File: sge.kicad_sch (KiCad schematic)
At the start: 23 parts, among them IC6 315-5660

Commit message: Enlarge some footprints, fix unwanted A/D ground connections.
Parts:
- IC6: footprint Package_QFP:LQFP-208_28x28mm_P0.5mm -> Neptune:QFP-208_28x28_Pitch0.5mm
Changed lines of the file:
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@@
       (effects (font (size 5 5)))
     )
-    (property "Footprint" "Package_QFP:LQFP-208_28x28mm_P0.5mm" (at 212.09 135.89 0)
+    (property "Footprint" "Neptune:QFP-208_28x28_Pitch0.5mm" (at 212.09 135.89 0)
       (effects (font (size 1.27 1.27)) hide)
     )

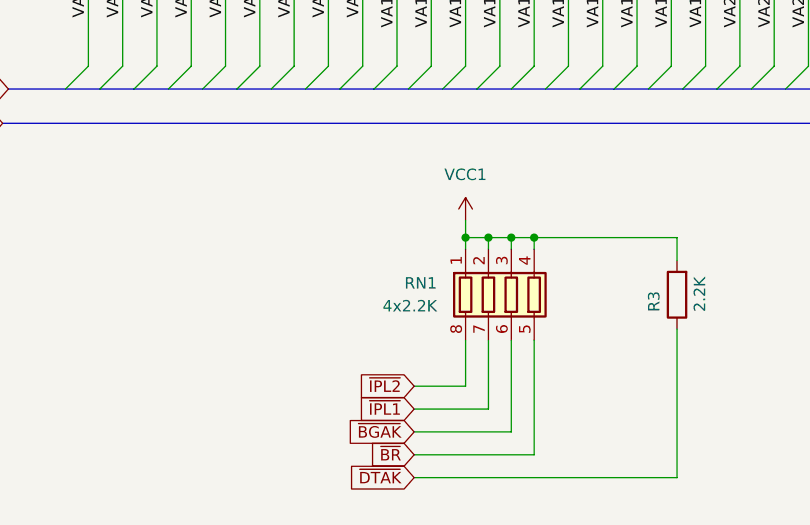
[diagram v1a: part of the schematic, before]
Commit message: Renumber "missing" resistor pack.
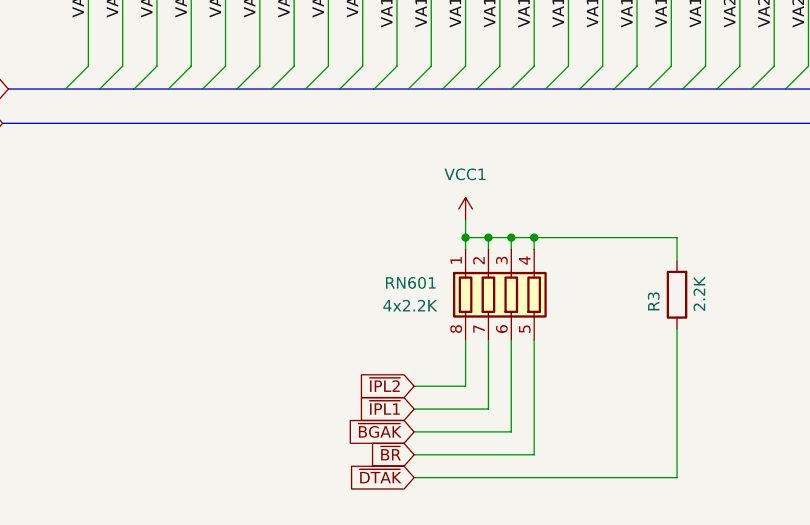
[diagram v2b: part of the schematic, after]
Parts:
- renumbered RN1 to RN601
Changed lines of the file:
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@@
   (symbol (lib_id "Device:R_Pack04") (at 127 256.54 0) (mirror x) (unit 1)
     (in_bom yes) (on_board yes) (dnp no)
-    (property "Reference" "RN1" (at 118.745 255.27 0)
+    (property "Reference" "RN601" (at 118.745 255.27 0)
       (effects (font (size 1.27 1.27)) (justify right))
     )
@@
       (project "Neptune"
         (path "/bcc23b51-b742-4ae5-9dd6-d96a24058944/0d895458-d3d0-4635-bde5-e15500822f5f"
-          (reference "RN1") (unit 1)
+          (reference "RN601") (unit 1)
         )
       )

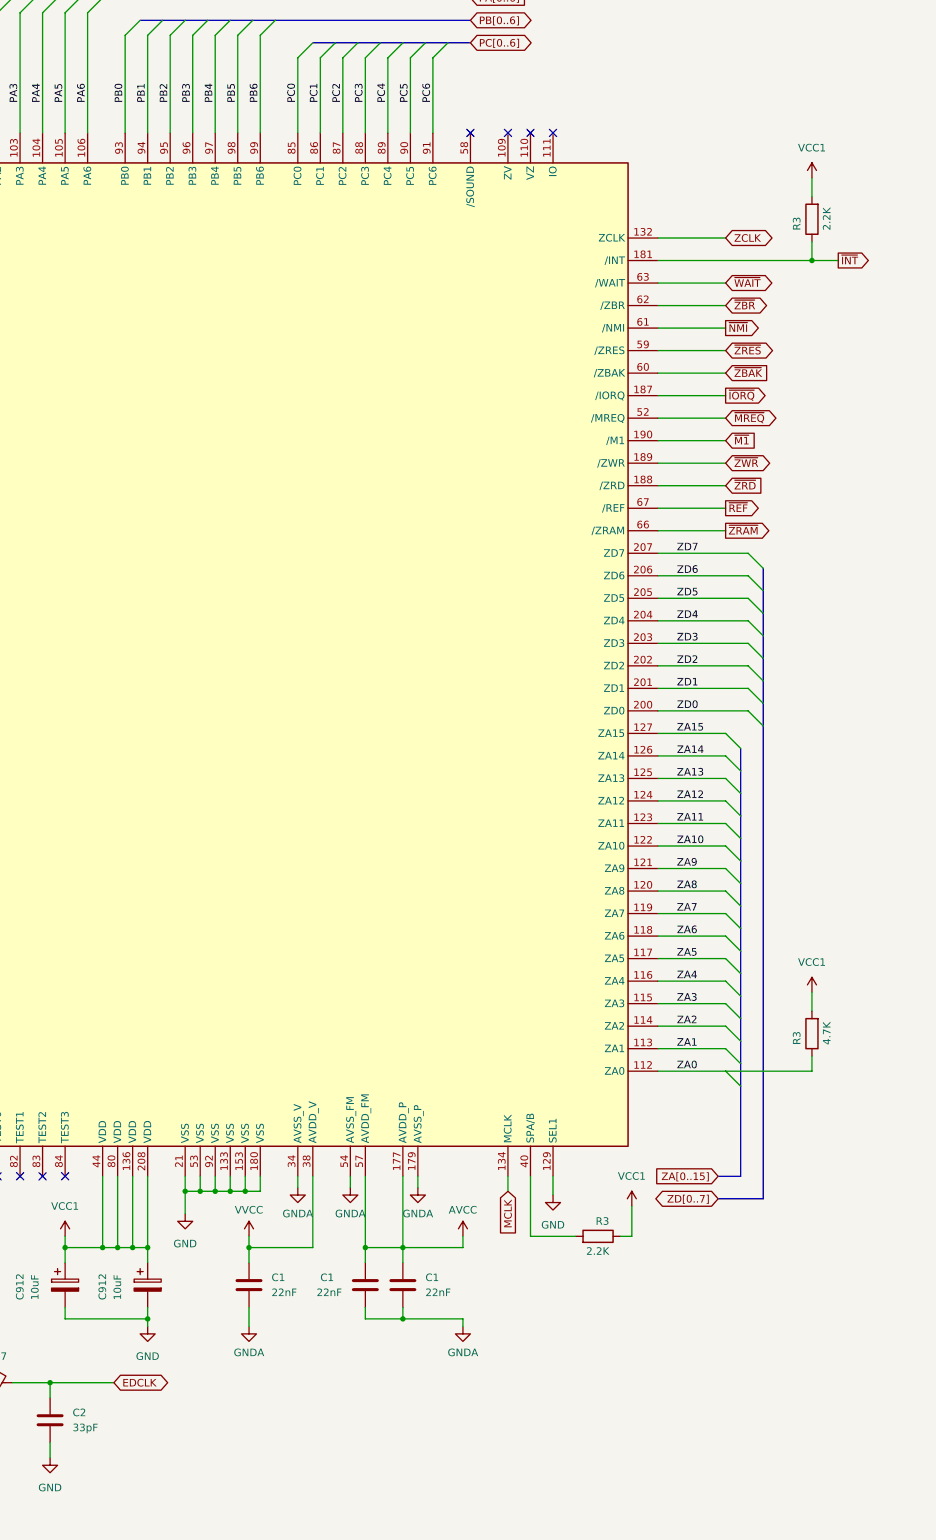
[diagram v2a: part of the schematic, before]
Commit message: Add/correct MD PAL timing caps.
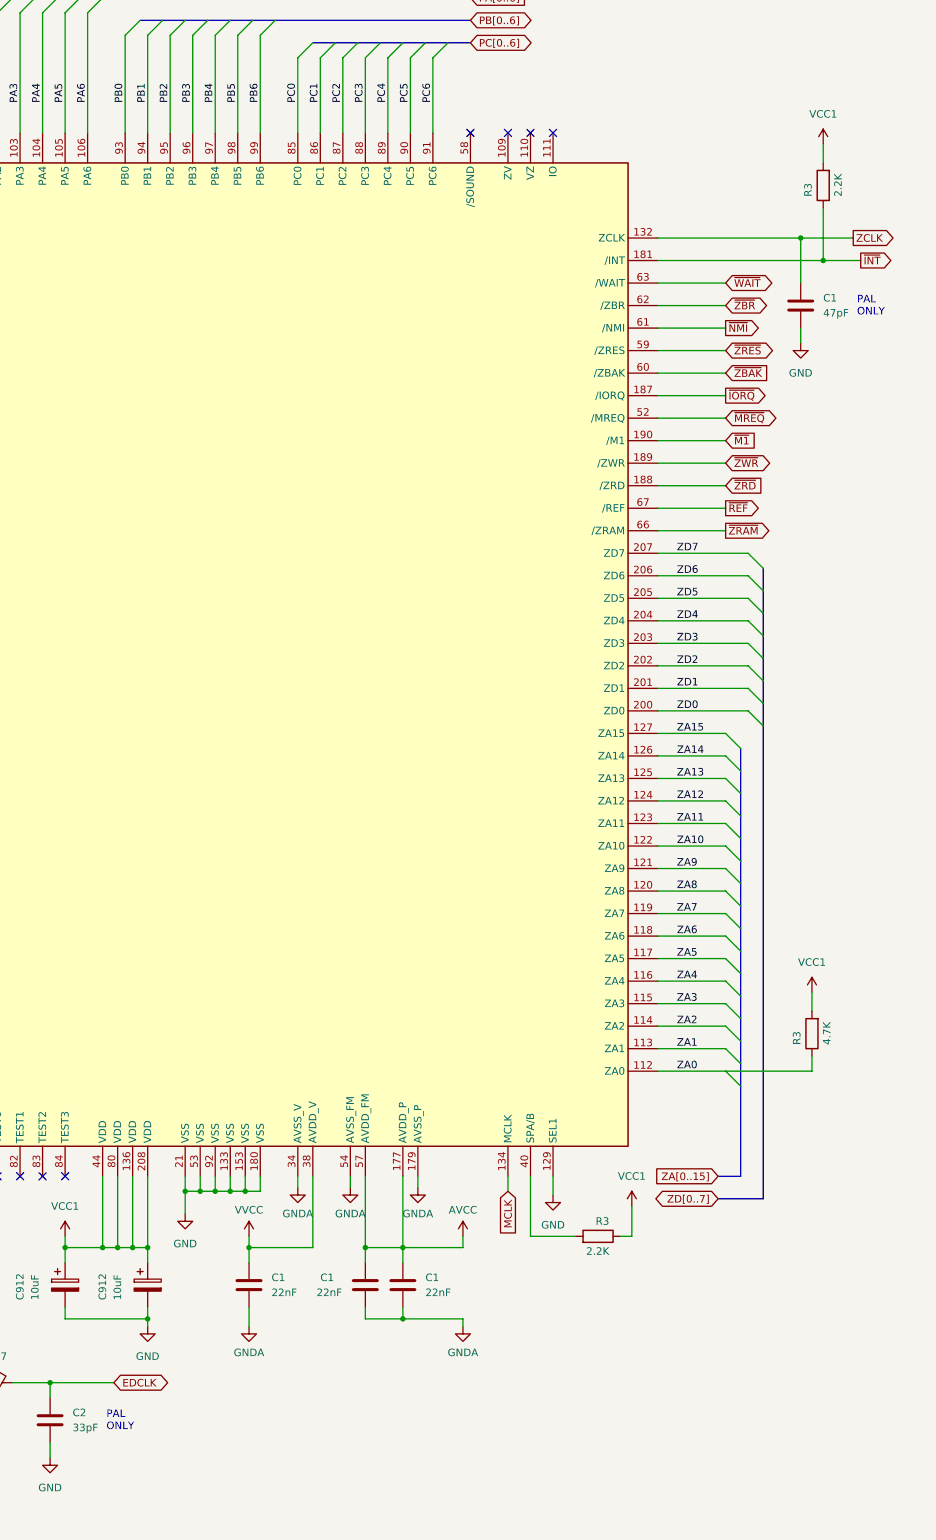
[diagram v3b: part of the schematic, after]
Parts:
- added C1: 47pF, Capacitor_SMD:C_0805_2012Metric, symbol Device:C
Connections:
- net GND: now also C1.2
- net ZCLK: now also C1.1
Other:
- note added: "PAL ONLY"
- moved on the sheet: R3
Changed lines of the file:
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@@
   (junction (at 121.92 250.19) (diameter 0) (color 0 0 0 0)
   )
+  (junction (at 388.62 60.96) (diameter 0) (color 0 0 0 0)
+  )
   (junction (at 264.16 231.775) (diameter 0) (color 0 0 0 0)
   )
@@
   (junction (at 275.59 231.775) (diameter 0) (color 0 0 0 0)
   )
-  (junction (at 390.525 64.77) (diameter 0) (color 0 0 0 0)
-  )
   (junction (at 127 250.19) (diameter 0) (color 0 0 0 0)
   )
@@
   (junction (at 278.13 231.775) (diameter 0) (color 0 0 0 0)
   )
+  (junction (at 392.43 64.77) (diameter 0) (color 0 0 0 0)
+  )
   (junction (at 273.05 231.775) (diameter 0) (color 0 0 0 0)
   )
@@
     (stroke (width 0) (type default))
   )
-  (wire (pts (xy 390.525 50.8) (xy 390.525 53.975))
+  (wire (pts (xy 392.43 45.085) (xy 392.43 48.26))
     (stroke (width 0) (type default))
   )
@@
     (stroke (width 0) (type default))
   )
+  (wire (pts (xy 392.43 64.77) (xy 398.78 64.77))
+    (stroke (width 0) (type default))
+  )
   (wire (pts (xy 215.9 40.005) (xy 215.9 43.18))
     (stroke (width 0) (type default))
   )
+  (wire (pts (xy 364.49 64.77) (xy 392.43 64.77))
+    (stroke (width 0) (type default))
+  )
   (wire (pts (xy 114.3 219.71) (xy 114.3 231.14))
     (stroke (width 0) (type default))
@@
     (stroke (width 0) (type default))
   )
-  (wire (pts (xy 364.49 60.96) (xy 375.92 60.96))
+  (wire (pts (xy 364.49 60.96) (xy 388.62 60.96))
     (stroke (width 0) (type default))
   )
@@
     (stroke (width 0) (type default))
   )
-  (wire (pts (xy 364.49 64.77) (xy 390.525 64.77))
-    (stroke (width 0) (type default))
-  )
   (bus (pts (xy 382.27 120.65) (xy 382.27 124.46))
     (stroke (width 0) (type default))
@@
     (stroke (width 0) (type default))
   )
+  (wire (pts (xy 388.62 76.2) (xy 388.62 78.74))
+    (stroke (width 0) (type default))
+  )
   (wire (pts (xy 113.03 41.91) (xy 113.03 43.18))
     (stroke (width 0) (type default))
@@
     (stroke (width 0) (type default))
   )
+  (wire (pts (xy 388.62 60.96) (xy 388.62 68.58))
+    (stroke (width 0) (type default))
+  )
   (wire (pts (xy 127 250.19) (xy 127 251.46))
     (stroke (width 0) (type default))
@@
     (stroke (width 0) (type default))
   )
-  (wire (pts (xy 390.525 64.77) (xy 394.97 64.77))
-    (stroke (width 0) (type default))
-  )
   (bus (pts (xy 114.3 20.32) (xy 110.49 20.32))
     (stroke (width 0) (type default))
@@
     (stroke (width 0) (type default))
   )
+  (wire (pts (xy 388.62 60.96) (xy 397.51 60.96))
+    (stroke (width 0) (type default))
+  )
   (bus (pts (xy 378.46 196.85) (xy 378.46 200.66))
     (stroke (width 0) (type default))
@@
     (stroke (width 0) (type default))
   )
-  (wire (pts (xy 390.525 61.595) (xy 390.525 64.77))
+  (wire (pts (xy 392.43 55.88) (xy 392.43 64.77))
     (stroke (width 0) (type default))
   )
@@
     (stroke (width 0) (type default))
   )
+  (text "PAL\nONLY" (at 398.145 74.295 0)
+    (effects (font (size 1.27 1.27)) (justify left bottom))
+  )
   (text "RA1-RA6: 100Ω" (at 152.4 39.37 0)
     (effects (font (size 1.27 1.27)) (justify left bottom))
   )
+  (text "PAL\nONLY" (at 271.145 262.89 0)
+    (effects (font (size 1.27 1.27)) (justify left bottom))
+  )
   (label "ZD7" (at 367.665 114.3 0) (fields_autoplaced)
     (effects (font (size 1.27 1.27)) (justify left bottom))
@@
     )
   )
-  (global_label "ZCLK" (shape bidirectional) (at 375.92 60.96 0) (fields_autoplaced)
+  (global_label "ZCLK" (shape output) (at 397.51 60.96 0) (fields_autoplaced)
     (effects (font (size 1.27 1.27)) (justify left))
-    (property "Intersheetrefs" "${INTERSHEET_REFS}" (at 384.7941 60.96 0)
+    (property "Intersheetrefs" "${INTERSHEET_REFS}" (at 405.2728 60.96 0)
       (effects (font (size 1.27 1.27)) (justify left) hide)
     )
@@
     )
   )
-  (global_label "~{INT}" (shape output) (at 394.97 64.77 0) (fields_autoplaced)
+  (global_label "~{INT}" (shape output) (at 398.78 64.77 0) (fields_autoplaced)
     (effects (font (size 1.27 1.27)) (justify left))
-    (property "Intersheetrefs" "${INTERSHEET_REFS}" (at 400.8581 64.77 0)
+    (property "Intersheetrefs" "${INTERSHEET_REFS}" (at 404.6681 64.77 0)
       (effects (font (size 1.27 1.27)) (justify left) hide)
     )
@@
     )
   )
+  (symbol (lib_id "power:GND") (at 388.62 78.74 0) (unit 1)
+    (in_bom yes) (on_board yes) (dnp no) (fields_autoplaced)
+    (property "Reference" "#PWR095" (at 388.62 85.09 0)
+      (effects (font (size 1.27 1.27)) hide)
+    )
+    (property "Value" "GND" (at 388.62 83.82 0)
+      (effects (font (size 1.27 1.27)))
+    )
+    (property "Footprint" "" (at 388.62 78.74 0)
+      (effects (font (size 1.27 1.27)) hide)
+    )
+    (property "Datasheet" "" (at 388.62 78.74 0)
+      (effects (font (size 1.27 1.27)) hide)
+    )
+    (pin "1")
+    (instances
+      (project "Neptune"
+        (path "/bcc23b51-b742-4ae5-9dd6-d96a24058944/0d895458-d3d0-4635-bde5-e15500822f5f"
+          (reference "#PWR095") (unit 1)
+        )
+      )
+    )
+  )
   (symbol (lib_id "Device:R_Pack04_Split") (at 198.12 38.1 0) (mirror x) (unit 2)
     (in_bom yes) (on_board yes) (dnp no)
@@
         )
         (path "/bcc23b51-b742-4ae5-9dd6-d96a24058944/0d895458-d3d0-4635-bde5-e15500822f5f"
-          (reference "C22") (unit 1)
+          (reference "C11") (unit 1)
         )
       )
@@
     )
   )
-  (symbol (lib_id "Device:R") (at 390.525 57.785 180) (unit 1)
+  (symbol (lib_id "Device:R") (at 392.43 52.07 180) (unit 1)
     (in_bom yes) (on_board yes) (dnp no)
-    (property "Reference" "R3" (at 387.985 59.69 90)
+    (property "Reference" "R3" (at 389.89 53.975 90)
       (effects (font (size 1.27 1.27)) (justify right))
     )
-    (property "Value" "2.2K" (at 393.065 59.69 90)
+    (property "Value" "2.2K" (at 394.97 53.975 90)
       (effects (font (size 1.27 1.27)) (justify right))
     )
-    (property "Footprint" "Resistor_SMD:R_0805_2012Metric" (at 392.303 57.785 90)
+    (property "Footprint" "Resistor_SMD:R_0805_2012Metric" (at 394.208 52.07 90)
       (effects (font (size 1.27 1.27)) hide)
     )
-    (property "Datasheet" "~" (at 390.525 57.785 0)
+    (property "Datasheet" "~" (at 392.43 52.07 0)
       (effects (font (size 1.27 1.27)) hide)
     )
-    (property "DigiKey" "P2.20KCCT-ND" (at 390.525 57.785 0)
+    (property "DigiKey" "P2.20KCCT-ND" (at 392.43 52.07 0)
       (effects (font (size 1.27 1.27)) hide)
     )
@@
     )
   )
-  (symbol (lib_id "MegaDrive:VCC1") (at 390.525 50.8 0) (unit 1)
+  (symbol (lib_id "MegaDrive:VCC1") (at 392.43 45.085 0) (unit 1)
     (in_bom yes) (on_board yes) (dnp no) (fields_autoplaced)
-    (property "Reference" "#PWR01" (at 390.525 54.61 0)
+    (property "Reference" "#PWR01" (at 392.43 48.895 0)
       (effects (font (size 1.27 1.27)) hide)
     )
-    (property "Value" "VCC1" (at 390.525 45.72 0)
+    (property "Value" "VCC1" (at 392.43 40.005 0)
       (effects (font (size 1.27 1.27)))
     )
-    (property "Footprint" "" (at 390.525 50.8 0)
+    (property "Footprint" "" (at 392.43 45.085 0)
       (effects (font (size 1.27 1.27)) hide)
     )
-    (property "Datasheet" "" (at 390.525 50.8 0)
+    (property "Datasheet" "" (at 392.43 45.085 0)
       (effects (font (size 1.27 1.27)) hide)
     )
@@
         )
       )
+    )
+  )
+  (symbol (lib_id "Device:C") (at 388.62 72.39 0) (unit 1)
+    (in_bom yes) (on_board yes) (dnp no) (fields_autoplaced)
+    (property "Reference" "C1" (at 392.43 71.12 0)
+      (effects (font (size 1.27 1.27)) (justify left))
+    )
+    (property "Value" "47pF" (at 392.43 73.66 0)
+      (effects (font (size 1.27 1.27)) (justify left))
+    )
+    (property "Footprint" "Capacitor_SMD:C_0805_2012Metric" (at 389.5852 76.2 0)
+      (effects (font (size 1.27 1.27)) hide)
+    )
+    (property "Datasheet" "~" (at 388.62 72.39 0)
+      (effects (font (size 1.27 1.27)) hide)
+    )
+    (property "DigiKey" "" (at 388.62 72.39 0)
+      (effects (font (size 1.27 1.27)) hide)
+    )
+    (pin "1")
+    (pin "2")
+    (instances
+      (project "Neptune"
+        (path "/bcc23b51-b742-4ae5-9dd6-d96a24058944/01513199-62c5-4123-a151-ccd381a5e6c1"
+          (reference "C1") (unit 1)
+        )
+        (path "/bcc23b51-b742-4ae5-9dd6-d96a24058944/0d895458-d3d0-4635-bde5-e15500822f5f"
+          (reference "C9") (unit 1)
+        )
+      )

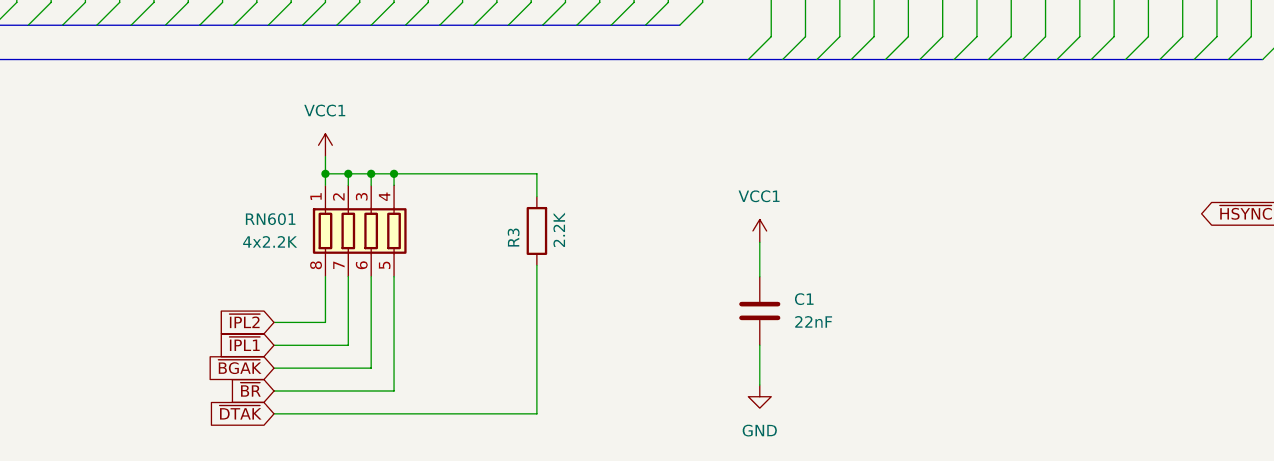
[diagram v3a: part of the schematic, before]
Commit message: Extra decoupling for IC6, use original RA8.
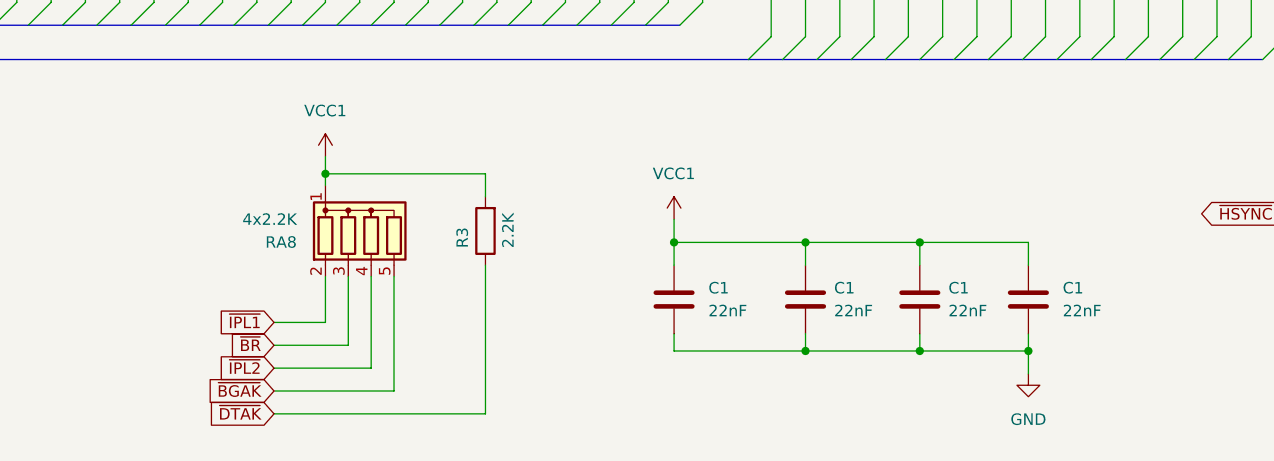
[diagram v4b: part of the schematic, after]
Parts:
- added C1 (x3): 22nF, Capacitor_SMD:C_0805_2012Metric, symbol Device:C
- RA8: renamed from RN601; footprint Resistor_SMD:R_Array_Convex_4x0603 -> Neptune:RA_4_Common; symbol Device:R_Pack04 -> Device:R_Network04
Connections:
- net GND: now also C1.2, C1.2, C1.2
- net VCC1: now also C1.1, C1.1, C1.1; no longer RA8.2 (R2.1), RA8.3 (R3.1), RA8.4 (R4.1)
- net ~{BGAK}: now also RA8.5 (R4); no longer RA8.6 (R3.2)
- net ~{BR}: now also RA8.3 (R2); no longer RA8.5 (R4.2)
- net ~{IPL1}: now also RA8.2 (R1); no longer RA8.7 (R2.2)
- net ~{IPL2}: now also RA8.4 (R3); no longer RA8.8 (R1.2)
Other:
- moved on the sheet: C1, R3

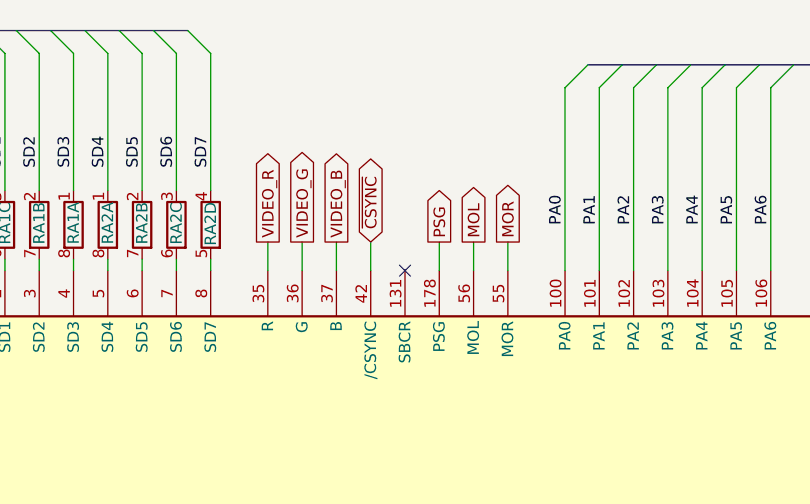
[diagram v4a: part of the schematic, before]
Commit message: Hook up SBCR (subcarrier) to 32X video encoder.
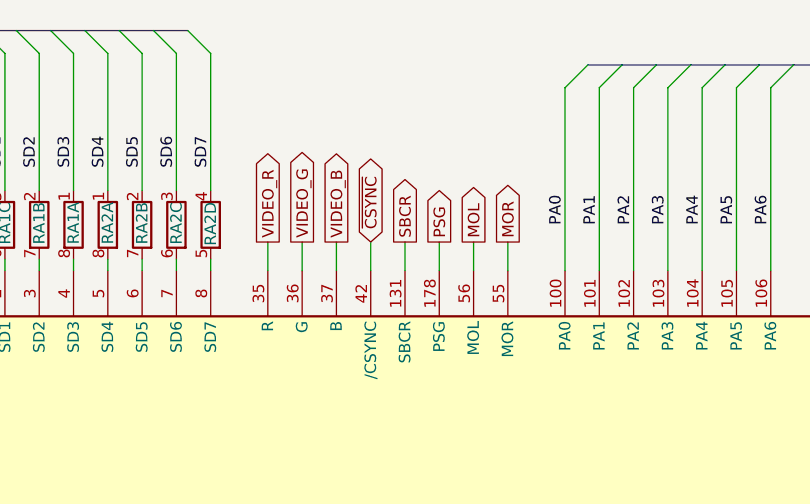
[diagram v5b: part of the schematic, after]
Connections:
- net SBCR: now reaches IC6.131 (SBCR)
- no-connect marks 19 -> 18
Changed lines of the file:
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@@
   (no_connect (at 146.05 43.18))
   (no_connect (at 87.63 43.18))
-  (no_connect (at 227.33 43.18))
   (no_connect (at 252.73 219.71))
   (no_connect (at 168.91 43.18))
@@
     (stroke (width 0) (type default))
   )
+  (wire (pts (xy 227.33 40.005) (xy 227.33 43.18))
+    (stroke (width 0) (type default))
+  )
   (wire (pts (xy 200.025 269.875) (xy 200.025 267.97))
     (stroke (width 0) (type default))
@@
     )
   )
+  (global_label "SBCR" (shape output) (at 227.33 40.005 90) (fields_autoplaced)
+    (effects (font (size 1.27 1.27)) (justify left))
+    (property "Intersheetrefs" "${INTERSHEET_REFS}" (at 227.33 32.0003 90)
+      (effects (font (size 1.27 1.27)) (justify left) hide)
+    )
+  )
